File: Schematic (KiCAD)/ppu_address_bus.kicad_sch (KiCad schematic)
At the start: 60 parts, among them X3 INVERT

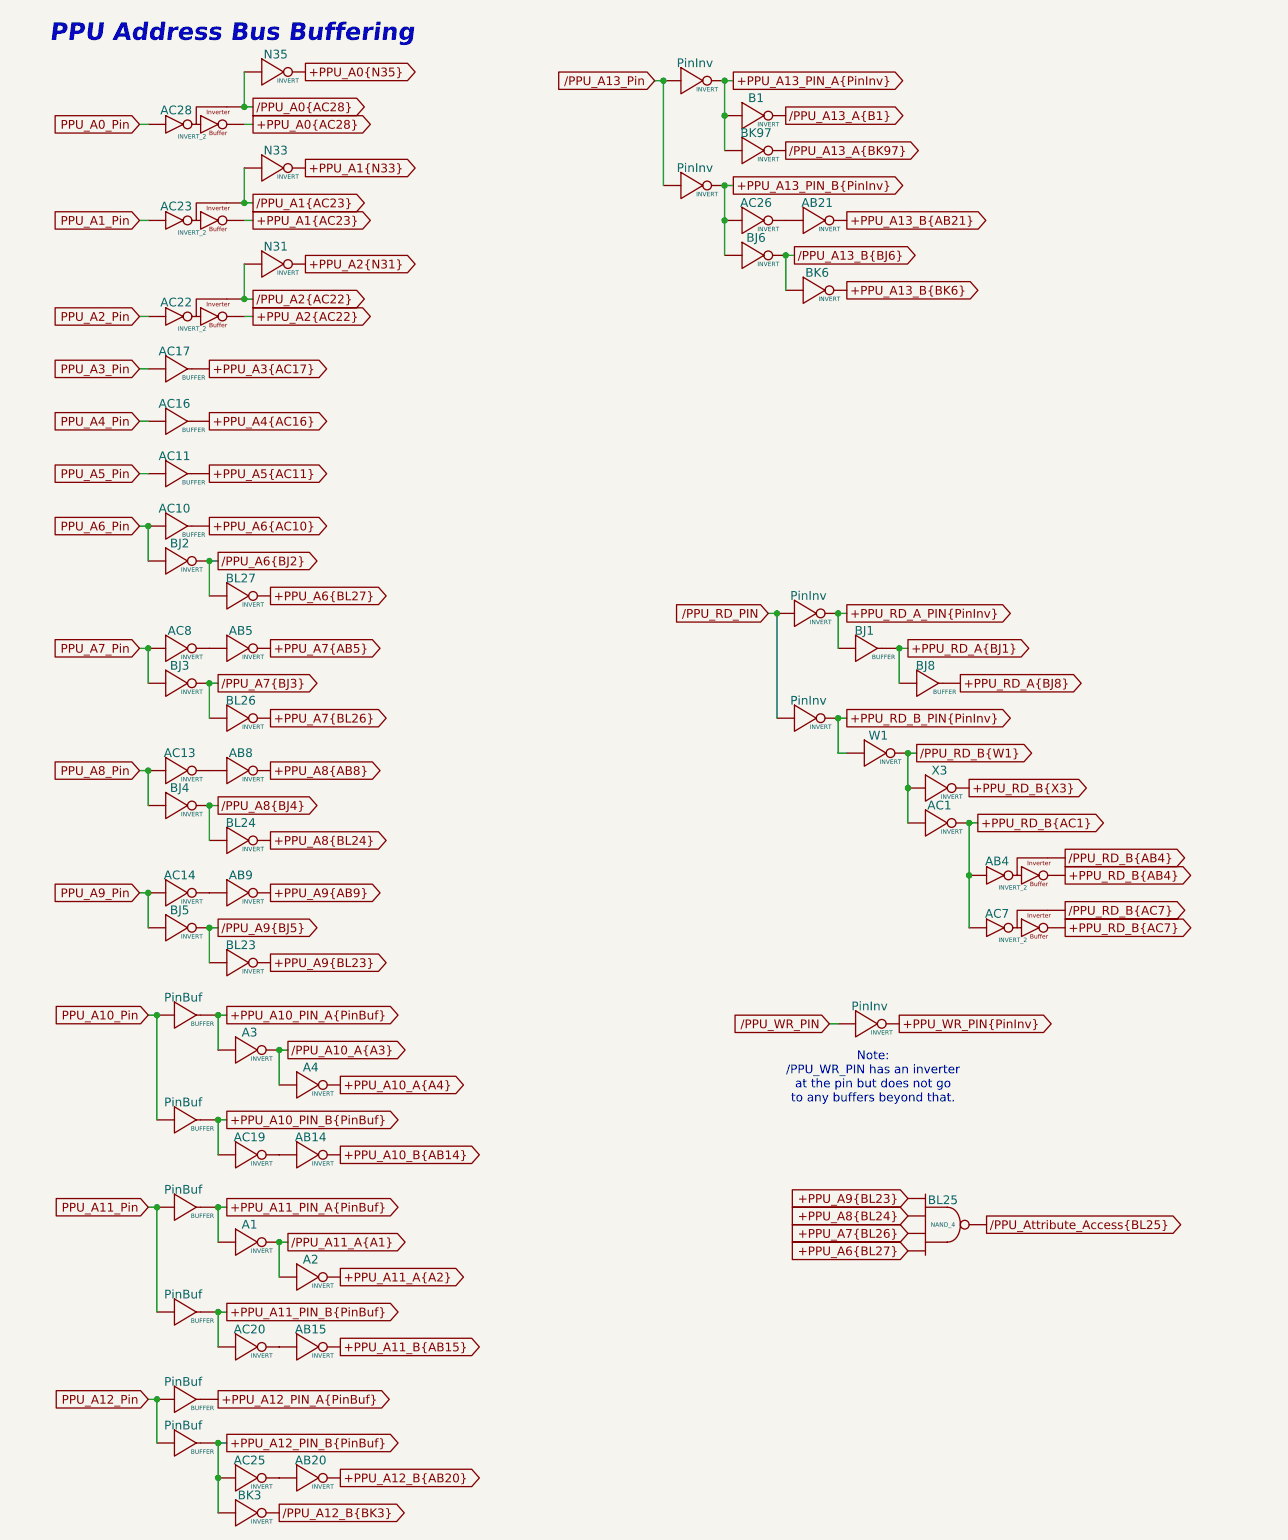
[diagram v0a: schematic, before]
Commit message: Tracing and schematic updates.  - Added timer to schematic.  - Added all items from artifacts sheet to the MMC5A trace.
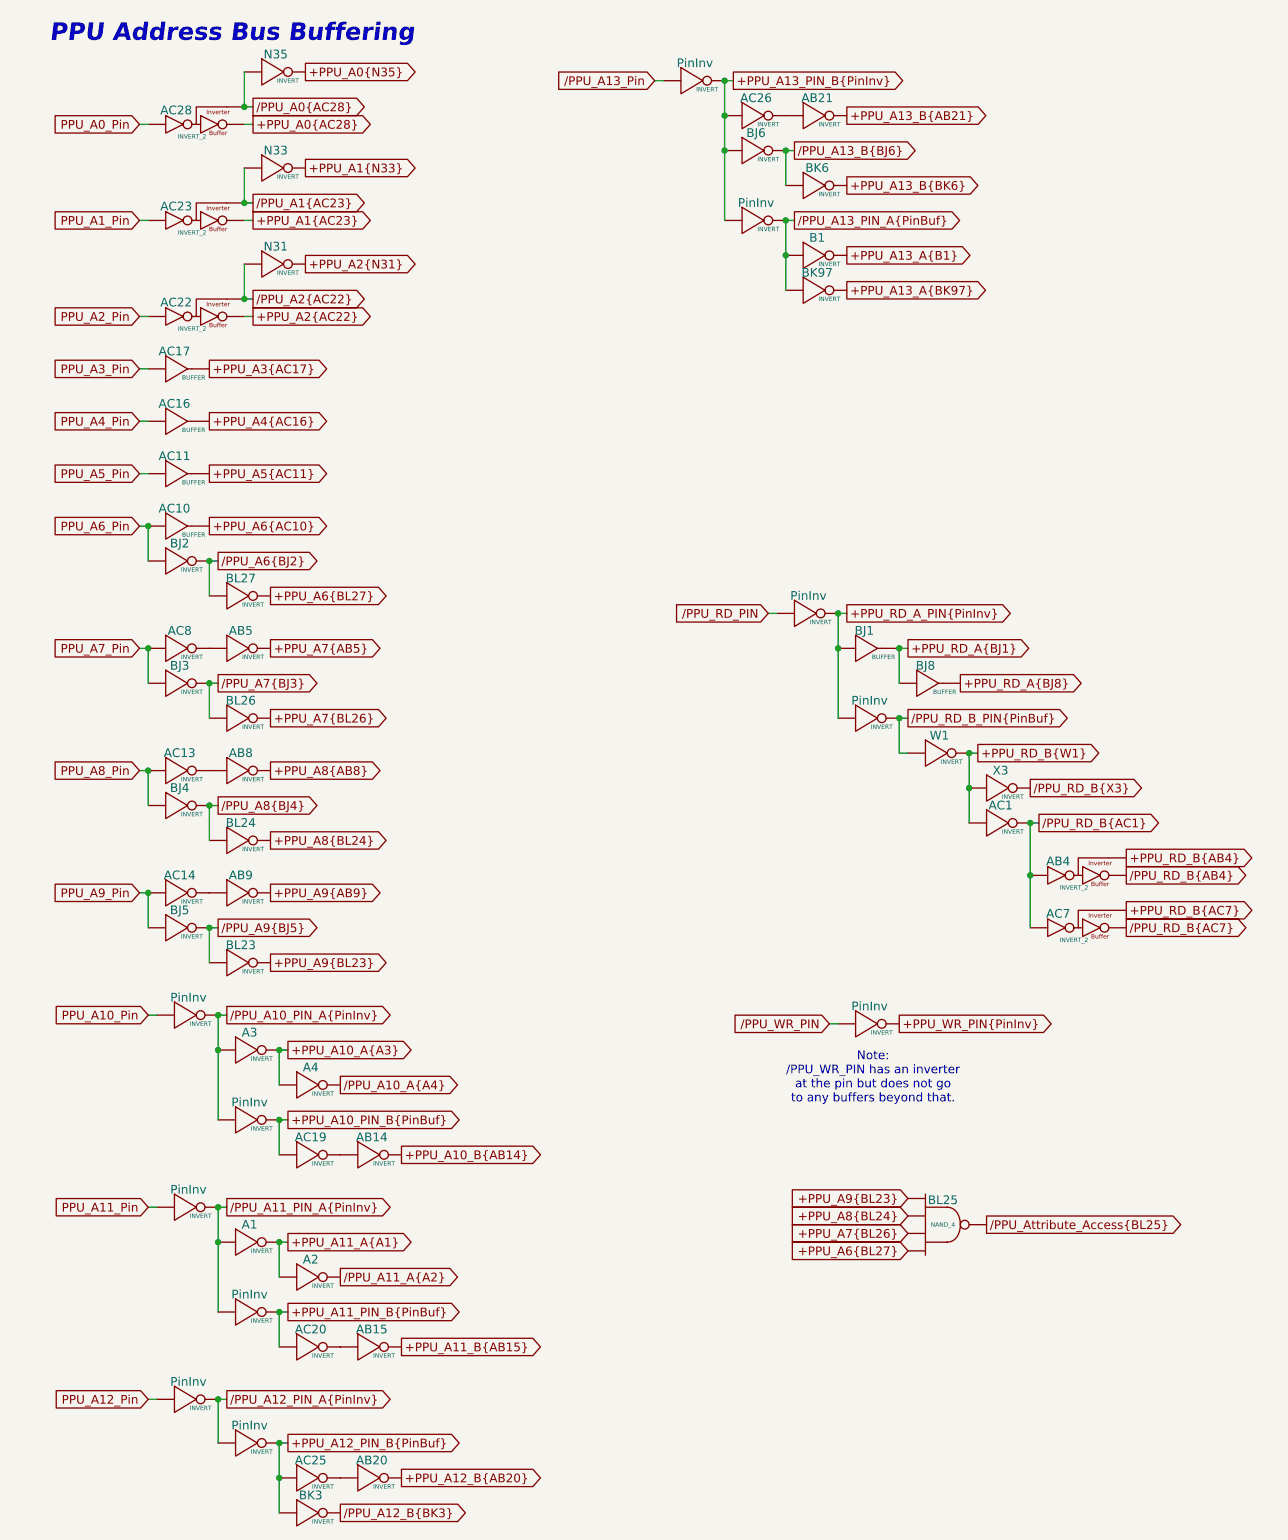
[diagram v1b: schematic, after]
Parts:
- removed PinBuf (x6): BUFFER, symbol MMC5:BUFFER
- added PinInv (x6): INVERT, symbol MMC5:INVERT
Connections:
- net /PPU_A13_A{B1} is gone; now on net /PPU_A13_PIN_A{PinBuf}: B1. (X)
- net /PPU_A13_A{BK97} is gone; now on net /PPU_A13_PIN_A{PinBuf}: BK97. (X)
- net +PPU_A10_PIN_B{PinBuf}: now also PinInv. (X)
- net +PPU_A11_PIN_B{PinBuf}: now also PinInv. (X)
- net +PPU_A12_PIN_B{PinBuf}: now also PinInv. (X)
- net +PPU_A13_PIN_B{PinInv}: now also PinInv. (X)
- net +PPU_RD_A_PIN{PinInv}: now also PinInv. (X)
- net PPU_A10_Pin: now also PinInv. (X)
- net PPU_A11_Pin: now also PinInv. (X)
- net PPU_A12_Pin: now also PinInv. (X)
- net /PPU_A13_Pin: no longer PinInv. (X)
- net /PPU_RD_PIN: no longer PinInv. (X)
- net +PPU_A10_A{A4} renamed /PPU_A10_A{A4}
- net +PPU_A10_PIN_A{PinBuf} renamed /PPU_A10_PIN_A{PinInv}
- net /PPU_A10_PIN_A{PinInv}: now also PinInv. (X), PinInv. (X)
- net +PPU_A11_A{A2} renamed /PPU_A11_A{A2}
- net +PPU_A11_PIN_A{PinBuf} renamed /PPU_A11_PIN_A{PinInv}
- net /PPU_A11_PIN_A{PinInv}: now also PinInv. (X), PinInv. (X)
- net +PPU_A13_PIN_A{PinInv} renamed /PPU_A13_PIN_A{PinBuf}
- net +PPU_RD_B_PIN{PinInv} renamed /PPU_RD_B_PIN{PinBuf}
- net +PPU_RD_B{AC1} renamed /PPU_RD_B{AC1}
- net +PPU_RD_B{X3} renamed /PPU_RD_B{X3}
- removed net /PPU_A10_A{A3}: A3. (X), A4. (X)
- removed net /PPU_A11_A{A1}: A1. (X), A2. (X)
- removed net /PPU_RD_B{W1}: AC1. (X), W1. (X), X3. (X)
- new net: AB21. (X), AC26. (X)
- new net: AB15. (X), AC20. (X)
- new net: AB5. (X), AC8. (X)
- new net: AB9. (X), AC14. (X)
- new net: AB20. (X), AC25. (X)
- new net: AB14. (X), AC19. (X)
- new net: AB8. (X), AC13. (X)
- new net +PPU_A10_A{A3}: A3. (X), A4. (X)
- new net +PPU_A11_A{A1}: A1. (X), A2. (X)
- new net +PPU_A13_A{B1}: B1. (X)
- new net +PPU_A13_A{BK97}: BK97. (X)
- new net +PPU_RD_B{W1}: AC1. (X), W1. (X), X3. (X)
- new net /PPU_A12_PIN_A{PinInv}: PinInv. (X), PinInv. (X)
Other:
- moved on the sheet: AB14, AB15, AB20, AB21, AB4, AC1, AC19, AC20, AC25, AC26, AC7, B1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

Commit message: - Updated all of the various And-OR-Invert gates to have consistent names.  - Added the schematic for CL3 / SL3 GPIO pins.  There are no surprises revealed by this.  - Finished up the CPU address decoding tracing.  - Added one of the 'artifact' counters from the pulse channels
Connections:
- new net: AB21. (X), AC26. (X)
- new net: AB15. (X), AC20. (X)
- new net: AB5. (X), AC8. (X)
- new net: AB9. (X), AC14. (X)
- new net: AB20. (X), AC25. (X)
- new net: AB14. (X), AC19. (X)
- new net: AB8. (X), AC13. (X)
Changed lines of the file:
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@@
 	)
 	(symbol
-		(lib_name "INVERT_33")
+		(lib_name "INVERT_31")
 		(lib_id "MMC5:INVERT")
 		(at 119.38 33.02 0)
@@
 	)
 	(symbol
-		(lib_name "INVERT_2_1")
+		(lib_name "INVERT_2_2")
 		(lib_id "MMC5:INVERT_2")
 		(at 36.83 43.18 0)
@@
 	)
 	(symbol
-		(lib_name "INVERT_31")
+		(lib_name "INVERT_32")
 		(lib_id "MMC5:INVERT")
 		(at 119.38 27.94 0)
@@
 	)
 	(symbol
-		(lib_name "BUFFER_11")
+		(lib_name "BUFFER_4")
 		(lib_id "MMC5:BUFFER")
 		(at 143.51 110.49 0)
@@
 	)
 	(symbol
-		(lib_name "INVERT_38")
+		(lib_name "INVERT_33")
 		(lib_id "MMC5:INVERT")
 		(at 135.89 160.02 0)
@@
 	)
 	(symbol
+		(lib_name "INVERT_2_4")
 		(lib_id "MMC5:INVERT_2")
 		(at 36.83 29.21 0)
@@
 	)
 	(symbol
-		(lib_name "INVERT_8")
+		(lib_name "INVERT_40")
 		(lib_id "MMC5:INVERT")
 		(at 49.53 35.56 0)
@@
 	)
 	(symbol
-		(lib_name "INVERT_45")
+		(lib_name "INVERT_42")
 		(lib_id "MMC5:INVERT")
 		(at 36.83 186.69 0)
@@
 	)
 	(symbol
-		(lib_name "BUFFER_7")
+		(lib_name "BUFFER_5")
 		(lib_id "MMC5:BUFFER")
 		(at 34.29 72.39 0)
@@
 	)
 	(symbol
-		(lib_name "INVERT_19")
+		(lib_name "INVERT_36")
 		(lib_id "MMC5:INVERT")
 		(at 35.56 128.27 0)
@@
 	)
 	(symbol
-		(lib_name "INVERT_43")
+		(lib_name "INVERT_47")
 		(lib_id "MMC5:INVERT")
 		(at 45.72 220.98 0)
@@
 	)
 	(symbol
-		(lib_name "INVERT_39")
+		(lib_name "INVERT_37")
 		(lib_id "MMC5:INVERT")
 		(at 127 100.33 0)
@@
 	)
 	(symbol
-		(lib_name "INVERT_2_4")
+		(lib_name "INVERT_2_3")
 		(lib_id "MMC5:INVERT_2")
 		(at 165.1 146.05 0)
@@
 	)
 	(symbol
-		(lib_name "INVERT_3")
+		(lib_name "INVERT_34")
 		(lib_id "MMC5:INVERT")
 		(at 45.72 163.83 0)
@@
 	)
 	(symbol
-		(lib_name "INVERT_2")
+		(lib_name "INVERT_38")
 		(lib_id "MMC5:INVERT")
 		(at 45.72 191.77 0)
@@
 	)
 	(symbol
-		(lib_name "INVERT_4")
+		(lib_name "INVERT_39")
 		(lib_id "MMC5:INVERT")
 		(at 54.61 196.85 0)
@@
 	)
 	(symbol
-		(lib_name "INVERT_26")
+		(lib_name "INVERT_10")
 		(lib_id "MMC5:INVERT")
 		(at 63.5 207.01 0)
@@
 	)
 	(symbol
-		(lib_name "INVERT_40")
+		(lib_name "INVERT_13")
 		(lib_id "MMC5:INVERT")
 		(at 135.89 115.57 0)
@@
 	)
 	(symbol
-		(lib_name "INVERT_37")
+		(lib_name "INVERT_14")
 		(lib_id "MMC5:INVERT")
 		(at 154.94 130.81 0)
@@
 	)
 	(symbol
-		(lib_name "INVERT_42")
+		(lib_name "INVERT_46")
 		(lib_id "MMC5:INVERT")
 		(at 36.83 214.63 0)
@@
 	)
 	(symbol
-		(lib_name "INVERT_2_2")
 		(lib_id "MMC5:INVERT_2")
 		(at 36.83 57.15 0)
@@
 	)
 	(symbol
-		(lib_name "INVERT_17")
+		(lib_name "INVERT_9")
 		(lib_id "MMC5:INVERT")
 		(at 44.45 133.35 0)
@@
 	)
 	(symbol
-		(lib_name "INVERT_13")
+		(lib_name "INVERT_2")
 		(lib_id "MMC5:INVERT")
 		(at 44.45 105.41 0)
@@
 	)
 	(symbol
-		(lib_name "INVERT_44")
+		(lib_name "INVERT_43")
 		(lib_id "MMC5:INVERT")
 		(at 45.72 201.93 0)
@@
 	)
 	(symbol
-		(lib_name "INVERT_20")
+		(lib_name "INVERT_11")
 		(lib_id "MMC5:INVERT")
 		(at 44.45 151.13 0)
@@
 	)
 	(symbol
-		(lib_name "INVERT_29")
+		(lib_name "INVERT_16")
 		(lib_id "MMC5:INVERT")
 		(at 63.5 226.06 0)
@@
 	)
 	(symbol
-		(lib_name "NAND_4_1")
 		(lib_id "MMC5:NAND_4")
 		(at 146.05 189.23 0)
@@
 	)
 	(symbol
-		(lib_name "INVERT_25")
+		(lib_name "INVERT_21")
 		(lib_id "MMC5:INVERT")
 		(at 54.61 179.07 0)
@@
 	)
 	(symbol
-		(lib_name "BUFFER_9")
+		(lib_name "BUFFER_2")
 		(lib_id "MMC5:BUFFER")
 		(at 34.29 87.63 0)
@@
 	)
 	(symbol
-		(lib_name "INVERT_11")
+		(lib_name "INVERT_19")
 		(lib_id "MMC5:INVERT")
 		(at 44.45 97.79 0)
@@
 	)
 	(symbol
-		(lib_name "INVERT_46")
+		(lib_name "INVERT_45")
 		(lib_id "MMC5:INVERT")
 		(at 36.83 158.75 0)
@@
 	)
 	(symbol
-		(lib_name "INVERT_27")
+		(lib_name "INVERT_4")
 		(lib_id "MMC5:INVERT")
 		(at 54.61 207.01 0)
@@
 	)
 	(symbol
-		(lib_name "INVERT_36")
+		(lib_name "INVERT_1")
 		(lib_id "MMC5:INVERT")
 		(at 154.94 125.73 0)
@@
 	)
 	(symbol
-		(lib_name "INVERT_12")
+		(lib_name "INVERT_24")
 		(lib_id "MMC5:INVERT")
 		(at 35.56 105.41 0)
@@
 	)
 	(symbol
-		(lib_name "INVERT_34")
+		(lib_name "INVERT_6")
 		(lib_id "MMC5:INVERT")
 		(at 128.27 53.34 0)
@@
 	)
 	(symbol
-		(lib_name "INVERT_6")
+		(lib_name "INVERT_25")
 		(lib_id "MMC5:INVERT")
 		(at 128.27 48.26 0)
@@
 	)
 	(symbol
-		(lib_name "INVERT_47")
+		(lib_name "INVERT_44")
 		(lib_id "MMC5:INVERT")
 		(at 45.72 173.99 0)
@@
 	)
 	(symbol
-		(lib_name "INVERT_2_3")
+		(lib_name "INVERT_2_1")
 		(lib_id "MMC5:INVERT_2")
 		(at 165.1 138.43 0)
@@
 	)
 	(symbol
-		(lib_name "BUFFER_10")
+		(lib_name "BUFFER_1")
 		(lib_id "MMC5:BUFFER")
 		(at 134.62 105.41 0)
@@
 	)
 	(symbol
-		(lib_name "BUFFER_6")
+		(lib_name "BUFFER_3")
 		(lib_id "MMC5:BUFFER")
 		(at 34.29 64.77 0)
@@
 	)
 	(symbol
-		(lib_name "INVERT_30")
+		(lib_name "INVERT_7")
 		(lib_id "MMC5:INVERT")
 		(at 54.61 231.14 0)
@@
 	)
 	(symbol
-		(lib_name "INVERT_24")
+		(lib_name "INVERT_26")
 		(lib_id "MMC5:INVERT")
 		(at 63.5 179.07 0)
@@
 	)
 	(symbol
-		(lib_name "BUFFER_8")
 		(lib_id "MMC5:BUFFER")
 		(at 34.29 80.01 0)
@@
 	)
 	(symbol
-		(lib_name "INVERT_28")
+		(lib_name "INVERT_18")
 		(lib_id "MMC5:INVERT")
 		(at 54.61 226.06 0)
@@
 	)
 	(symbol
-		(lib_name "INVERT_21")
+		(lib_name "INVERT_27")
 		(lib_id "MMC5:INVERT")
 		(at 44.45 140.97 0)
@@
 	)
 	(symbol
-		(lib_name "INVERT_9")
+		(lib_name "INVERT_3")
 		(lib_id "MMC5:INVERT")
 		(at 49.53 49.53 0)
@@
 	)
 	(symbol
-		(lib_name "INVERT_32")
 		(lib_id "MMC5:INVERT")
 		(at 128.27 27.94 0)
@@
 	)
 	(symbol
-		(lib_name "INVERT_16")
+		(lib_name "INVERT_28")
 		(lib_id "MMC5:INVERT")
 		(at 44.45 123.19 0)
@@
 	)
 	(symbol
-		(lib_name "INVERT_18")
+		(lib_name "INVERT_29")
 		(lib_id "MMC5:INVERT")
 		(at 35.56 123.19 0)
@@
 	)
 	(symbol
-		(lib_name "INVERT_10")
+		(lib_name "INVERT_8")
 		(lib_id "MMC5:INVERT")
 		(at 35.56 92.71 0)
@@
 	)
 	(symbol
-		(lib_name "INVERT_22")
+		(lib_name "INVERT_30")
 		(lib_id "MMC5:INVERT")
 		(at 35.56 146.05 0)
@@
 	)
 	(symbol
-		(lib_name "INVERT_14")
+		(lib_name "INVERT_20")
 		(lib_id "MMC5:INVERT")
 		(at 35.56 110.49 0)
@@
 	)
 	(symbol
-		(lib_name "INVERT_1")
+		(lib_name "INVERT_12")
 		(lib_id "MMC5:INVERT")
 		(at 119.38 43.18 0)
@@
 	)
 	(symbol
-		(lib_name "INVERT_7")
+		(lib_name "INVERT_17")
 		(lib_id "MMC5:INVERT")
 		(at 49.53 21.59 0)
@@
 	)
 	(symbol
+		(lib_name "INVERT_22")
 		(lib_id "MMC5:INVERT")
 		(at 110.49 22.86 0)
